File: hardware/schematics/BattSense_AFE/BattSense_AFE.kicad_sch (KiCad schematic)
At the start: 6 parts, among them J1 Battery, J2 ESP32_ADC

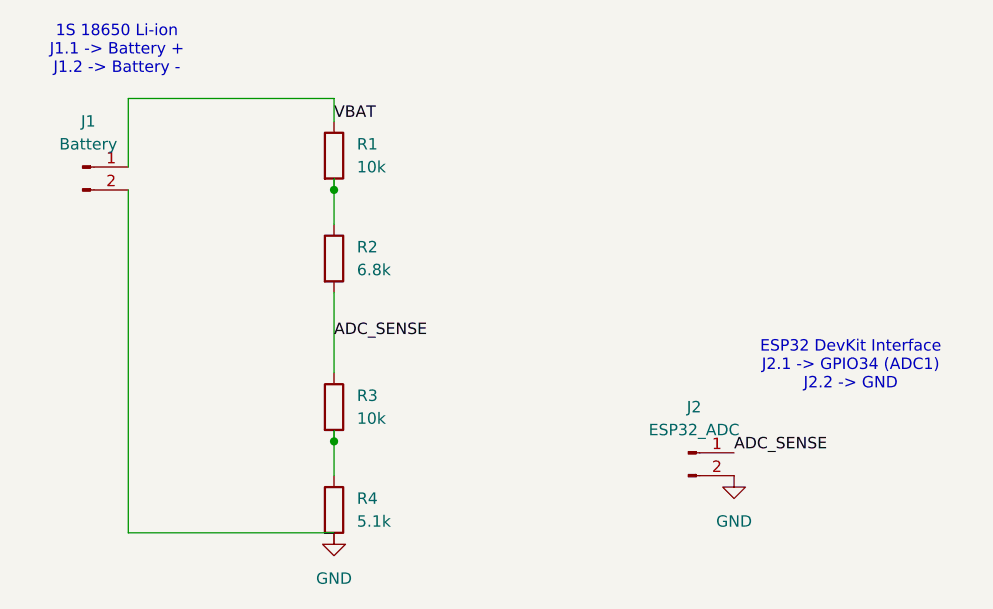
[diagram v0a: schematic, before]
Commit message: Revise analog front end to prevent ADC saturation
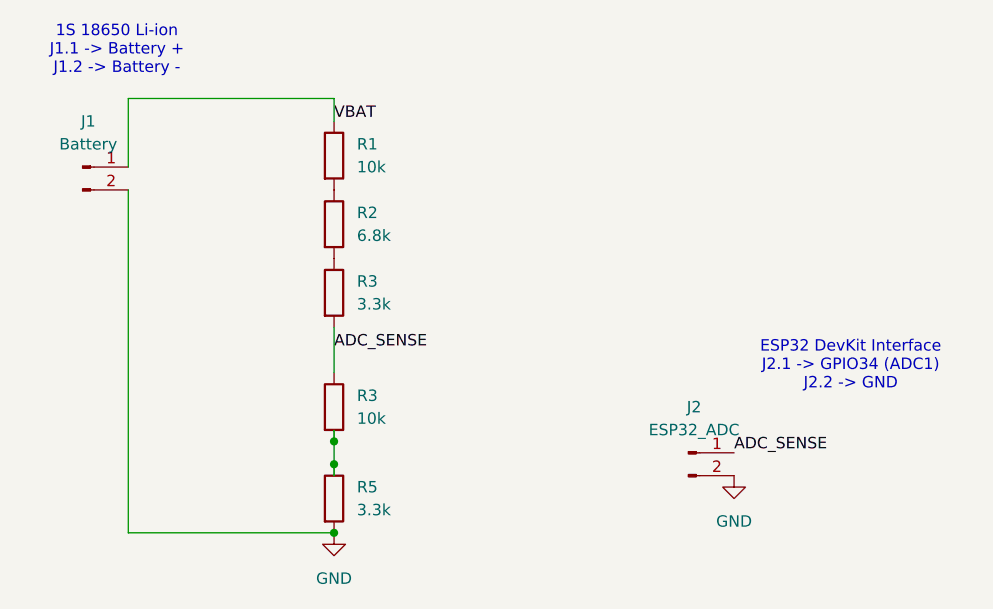
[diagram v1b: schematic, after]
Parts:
- removed R4: 5.1k, symbol Device:R
- added R3: 3.3k, Package_DIP:DIP-8_W7.62mm, symbol Device:R
- added R5: 3.3k, symbol Device:R
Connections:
- net ADC_SENSE: now also R3.2; no longer R2.2
- net GND: now also R5.2
- net at R3.2: now also R5.1
- new net: R2.2, R3.1
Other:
- moved on the sheet: R2
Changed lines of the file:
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@@
-	)
-	(junction
-		(at 63.5 39.37)
-		(diameter 0)
-		(color 0 0 0 0)
 	)
 	(junction
@@
 		(color 0 0 0 0)
 	)
+	(junction
+		(at 63.5 77.47)
+		(diameter 0)
+		(color 0 0 0 0)
+	)
+	(junction
+		(at 63.5 69.85)
+		(diameter 0)
+		(color 0 0 0 0)
+	)
 	(wire
 		(pts
@@
 	(wire
 		(pts
-			(xy 63.5 39.37) (xy 63.5 43.18)
-		)
-		(stroke
-			(width 0)
-			(type default)
-		)
-	)
-	(wire
-		(pts
-			(xy 63.5 38.1) (xy 63.5 39.37)
-		)
-		(stroke
-			(width 0)
-			(type default)
-		)
-	)
-	(wire
-		(pts
-			(xy 63.5 50.8) (xy 63.5 59.69)
+			(xy 63.5 69.85) (xy 63.5 71.12)
+		)
+		(stroke
+			(width 0)
+			(type default)
+		)
+	)
+	(wire
+		(pts
+			(xy 63.5 54.61) (xy 63.5 59.69)
 		)
 		(stroke
@@
 	(wire
 		(pts
-			(xy 63.5 67.31) (xy 63.5 71.12)
+			(xy 63.5 67.31) (xy 63.5 69.85)
 		)
 		(stroke
@@
 	)
 	(label "ADC_SENSE"
-		(at 63.5 55.88 0)
+		(at 63.5 57.15 0)
 		(effects
 			(font
@@
 			)
 			(justify left bottom)
+		)
+	)
+	(symbol
+		(lib_id "Device:R")
+		(at 63.5 50.8 0)
+		(unit 1)
+		(body_style 1)
+		(exclude_from_sim no)
+		(in_bom yes)
+		(on_board yes)
+		(in_pos_files yes)
+		(dnp no)
+		(fields_autoplaced yes)
+		(property "Reference" "R3"
+			(at 66.04 49.5299 0)
+			(show_name no)
+			(do_not_autoplace no)
+			(effects
+				(font
+					(size 1.27 1.27)
+				)
+				(justify left)
+			)
+		)
+		(property "Value" "3.3k"
+			(at 66.04 52.0699 0)
+			(show_name no)
+			(do_not_autoplace no)
+			(effects
+				(font
+					(size 1.27 1.27)
+				)
+				(justify left)
+			)
+		)
+		(property "Footprint" "Package_DIP:DIP-8_W7.62mm"
+			(at 61.722 50.8 90)
+			(hide yes)
+			(show_name no)
+			(do_not_autoplace no)
+			(effects
+				(font
+					(size 1.27 1.27)
+				)
+			)
+		)
+		(property "Datasheet" ""
+			(at 63.5 50.8 0)
+			(hide yes)
+			(show_name no)
+			(do_not_autoplace no)
+			(effects
+				(font
+					(size 1.27 1.27)
+				)
+			)
+		)
+		(property "Description" "Resistor"
+			(at 63.5 50.8 0)
+			(hide yes)
+			(show_name no)
+			(do_not_autoplace no)
+			(effects
+				(font
+					(size 1.27 1.27)
+				)
+			)
+		)
+		(pin "1"
+		)
+		(pin "2"
+		)
+		(instances
+			(project "BattSense_AFE"
+				(path "/332ccf2f-4d68-4237-9984-f4702488be93"
+					(reference "R3")
+					(unit 1)
+				)
+			)
 		)
 	)
@@
 	(symbol
 		(lib_id "Device:R")
-		(at 63.5 74.93 0)
-		(unit 1)
-		(body_style 1)
-		(exclude_from_sim no)
-		(in_bom yes)
-		(on_board yes)
-		(in_pos_files yes)
-		(dnp no)
-		(fields_autoplaced yes)
-		(property "Reference" "R4"
-			(at 66.04 73.6599 0)
-			(show_name no)
-			(do_not_autoplace no)
-			(effects
-				(font
-					(size 1.27 1.27)
-				)
-				(justify left)
-			)
-		)
-		(property "Value" "5.1k"
-			(at 66.04 76.1999 0)
-			(show_name no)
-			(do_not_autoplace no)
-			(effects
-				(font
-					(size 1.27 1.27)
-				)
-				(justify left)
-			)
-		)
-		(property "Footprint" ""
-			(at 61.722 74.93 90)
-			(hide yes)
-			(show_name no)
-			(do_not_autoplace no)
-			(effects
-				(font
-					(size 1.27 1.27)
-				)
-			)
-		)
-		(property "Datasheet" ""
-			(at 63.5 74.93 0)
-			(hide yes)
-			(show_name no)
-			(do_not_autoplace no)
-			(effects
-				(font
-					(size 1.27 1.27)
-				)
-			)
-		)
-		(property "Description" "Resistor"
-			(at 63.5 74.93 0)
-			(hide yes)
-			(show_name no)
-			(do_not_autoplace no)
-			(effects
-				(font
-					(size 1.27 1.27)
-				)
-			)
-		)
-		(pin "1"
-		)
-		(pin "2"
-		)
-		(instances
-			(project "BattSense_AFE"
-				(path "/332ccf2f-4d68-4237-9984-f4702488be93"
-					(reference "R4")
-					(unit 1)
-				)
-			)
-		)
-	)
-	(symbol
-		(lib_id "Device:R")
-		(at 63.5 46.99 0)
+		(at 63.5 43.18 0)
 		(unit 1)
 		(body_style 1)
@@
 		(fields_autoplaced yes)
 		(property "Reference" "R2"
-			(at 66.04 45.7199 0)
+			(at 66.04 41.9099 0)
 			(show_name no)
 			(do_not_autoplace no)
@@
 		)
 		(property "Value" "6.8k"
-			(at 66.04 48.2599 0)
+			(at 66.04 44.4499 0)
 			(show_name no)
 			(do_not_autoplace no)
@@
 		)
 		(property "Footprint" ""
-			(at 61.722 46.99 90)
+			(at 61.722 43.18 90)
 			(hide yes)
 			(show_name no)
@@
 		)
 		(property "Datasheet" ""
-			(at 63.5 46.99 0)
+			(at 63.5 43.18 0)
 			(hide yes)
 			(show_name no)
@@
 		)
 		(property "Description" "Resistor"
-			(at 63.5 46.99 0)
+			(at 63.5 43.18 0)
 			(hide yes)
 			(show_name no)
@@
 					(unit 1)
 				)
+			)
+		)
+	)
+	(symbol
+		(lib_id "Device:R")
+		(at 63.5 73.66 0)
+		(unit 1)
+		(body_style 1)
+		(exclude_from_sim no)
+		(in_bom yes)
+		(on_board yes)
+		(in_pos_files yes)
+		(dnp no)
+		(fields_autoplaced yes)
+		(property "Reference" "R5"
+			(at 66.04 72.3899 0)
+			(show_name no)
+			(do_not_autoplace no)
+			(effects
+				(font
+					(size 1.27 1.27)
+				)
+				(justify left)
+			)
+		)
+		(property "Value" "3.3k"
+			(at 66.04 74.9299 0)
+			(show_name no)
+			(do_not_autoplace no)
+			(effects
+				(font
+					(size 1.27 1.27)
+				)
+				(justify left)
+			)
+		)
+		(property "Footprint" ""
+			(at 61.722 73.66 90)
+			(hide yes)
+			(show_name no)
+			(do_not_autoplace no)
+			(effects
+				(font
+					(size 1.27 1.27)
+				)
+			)
+		)
+		(property "Datasheet" ""
+			(at 63.5 73.66 0)
+			(hide yes)
+			(show_name no)
+			(do_not_autoplace no)
+			(effects
+				(font
+					(size 1.27 1.27)
+				)
+			)
+		)
+		(property "Description" "Resistor"
+			(at 63.5 73.66 0)
+			(hide yes)
+			(show_name no)
+			(do_not_autoplace no)
+			(effects
+				(font
+					(size 1.27 1.27)
+				)
+			)
+		)
+		(pin "1"
+		)
+		(pin "2"
+		)
+		(instances
+			(project "BattSense_AFE"
+				(path "/332ccf2f-4d68-4237-9984-f4702488be93"
+					(reference "R5")
+					(unit 1)
+				)
